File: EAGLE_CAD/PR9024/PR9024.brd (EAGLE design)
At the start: 70 x 70 mm, 71 parts, among them SW1 C&K_PTS645

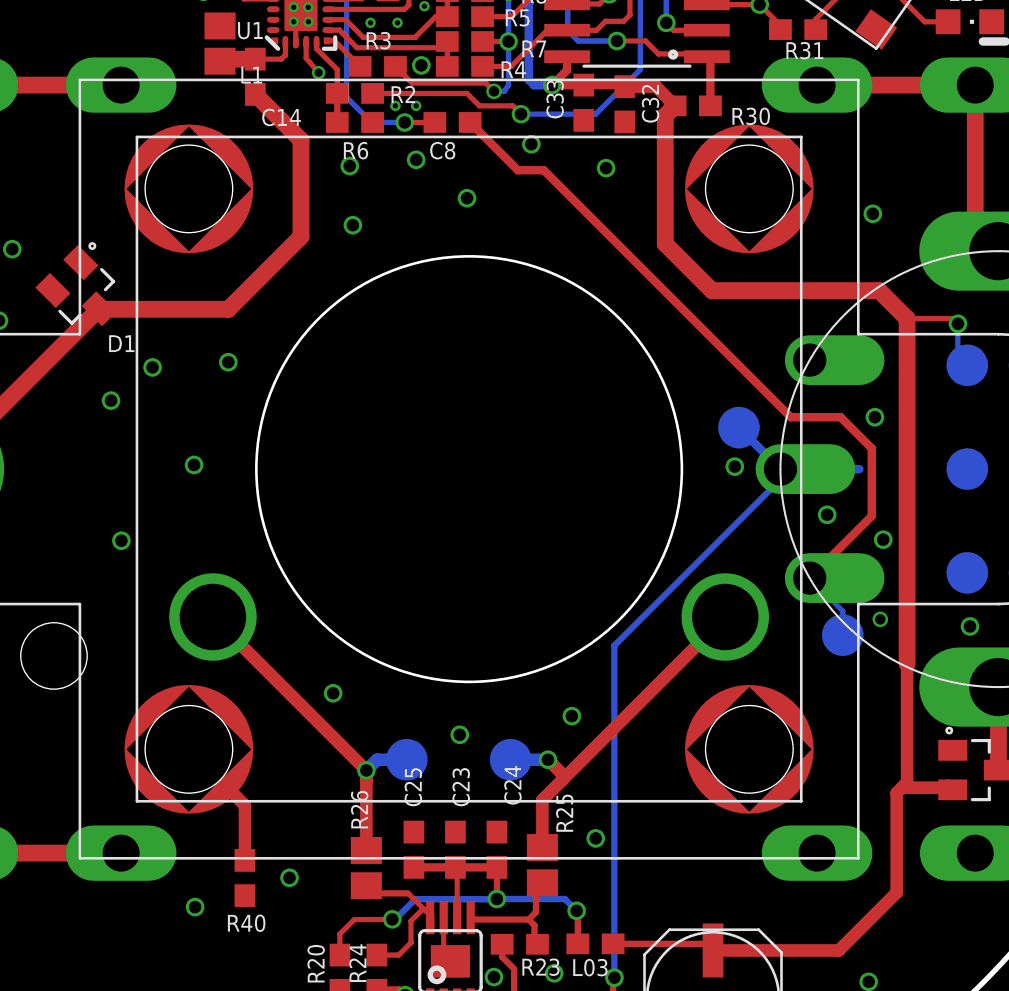
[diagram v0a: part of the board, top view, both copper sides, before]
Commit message: Updated Speaker Placement
Disconnected the SMT PEM nut placements from the speaker so the gerbers
reflect these as separate parts and placements.
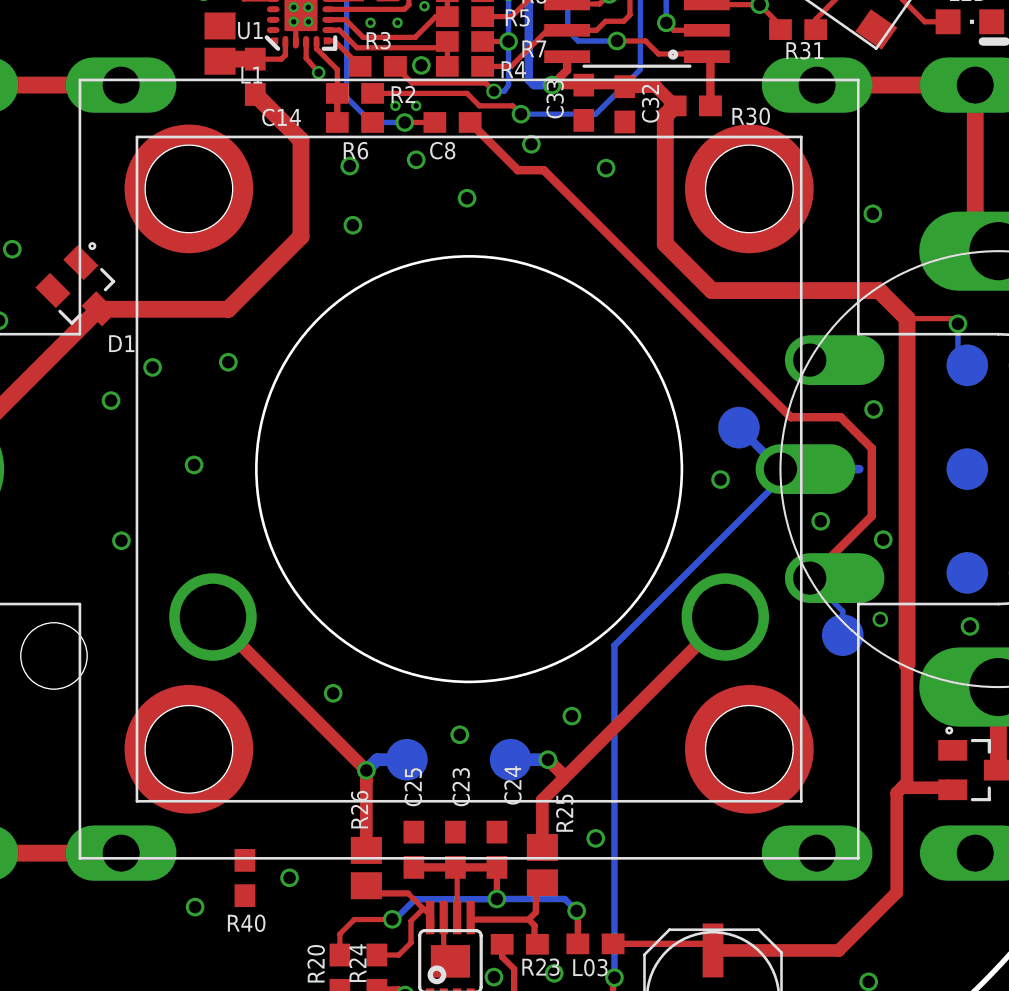
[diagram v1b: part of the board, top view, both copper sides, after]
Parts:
- added U$2, U$3, U$4, U$5: PEM_SMT, PR_Parts_Library:PEM_SMT
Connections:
- removed net N$6: R40.1, SPKR_PLACE.P$4
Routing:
- net N$6: track 6.47 -> 0.00 mm
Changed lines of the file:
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@@
 <attribute name="VALUE" x="32.336" y="14.891" size="1.27" layer="27" rot="R90"/>
 </element>
+<element name="U$2" library="PR_Parts_Library" package="PEM_SMT" value="PEM_SMT" x="21.5" y="48.5" locked="yes"/>
+<element name="U$3" library="PR_Parts_Library" package="PEM_SMT" value="PEM_SMT" x="48.5" y="48.5" locked="yes"/>
+<element name="U$4" library="PR_Parts_Library" package="PEM_SMT" value="PEM_SMT" x="48.5" y="21.5" locked="yes"/>
+<element name="U$5" library="PR_Parts_Library" package="PEM_SMT" value="PEM_SMT" x="21.5" y="21.5" locked="yes"/>
 </elements>
 <signals>
@@
 <via x="21.8" y="13.9" extent="1-16" drill="0.6"/>
 <via x="39.95" y="23.1" extent="1-16" drill="0.6"/>
-<via x="52.25" y="32.8" extent="1-16" drill="0.6"/>
+<via x="51.9375" y="32.4875" extent="1-16" drill="0.6"/>
 <via x="21.15375" y="64.95375" extent="1-16" drill="0.6"/>
 <contactref element="SW1" pad="P$1"/>
@@
 <via x="32.7" y="54.45" extent="1-16" drill="0.6"/>
 <via x="41.1" y="17.21" extent="1-16" drill="0.6"/>
-<via x="47.8" y="35.12" extent="1-16" drill="0.6"/>
-<via x="54.55" y="37.5" extent="1-16" drill="0.6"/>
+<via x="47.1125" y="34.495" extent="1-16" drill="0.6"/>
+<via x="54.4875" y="37.875" extent="1-16" drill="0.6"/>
 <via x="54.95" y="31.6" extent="1-16" drill="0.6"/>
 <via x="54.45" y="47.3" extent="1-16" drill="0.6"/>
@@
 <wire x1="30.55" y1="14.71" x2="30.7" y2="14.56" width="0.3048" layer="1"/>
 </signal>
-<signal name="N$6">
-<contactref element="SPKR_PLACE" pad="P$4"/>
-<contactref element="R40" pad="1"/>
-<wire x1="21.5" y1="21.5" x2="24.2" y2="18.8" width="0.6096" layer="1"/>
-<wire x1="24.2" y1="18.8" x2="24.2" y2="16.15" width="0.6096" layer="1"/>
-</signal>
 </signals>

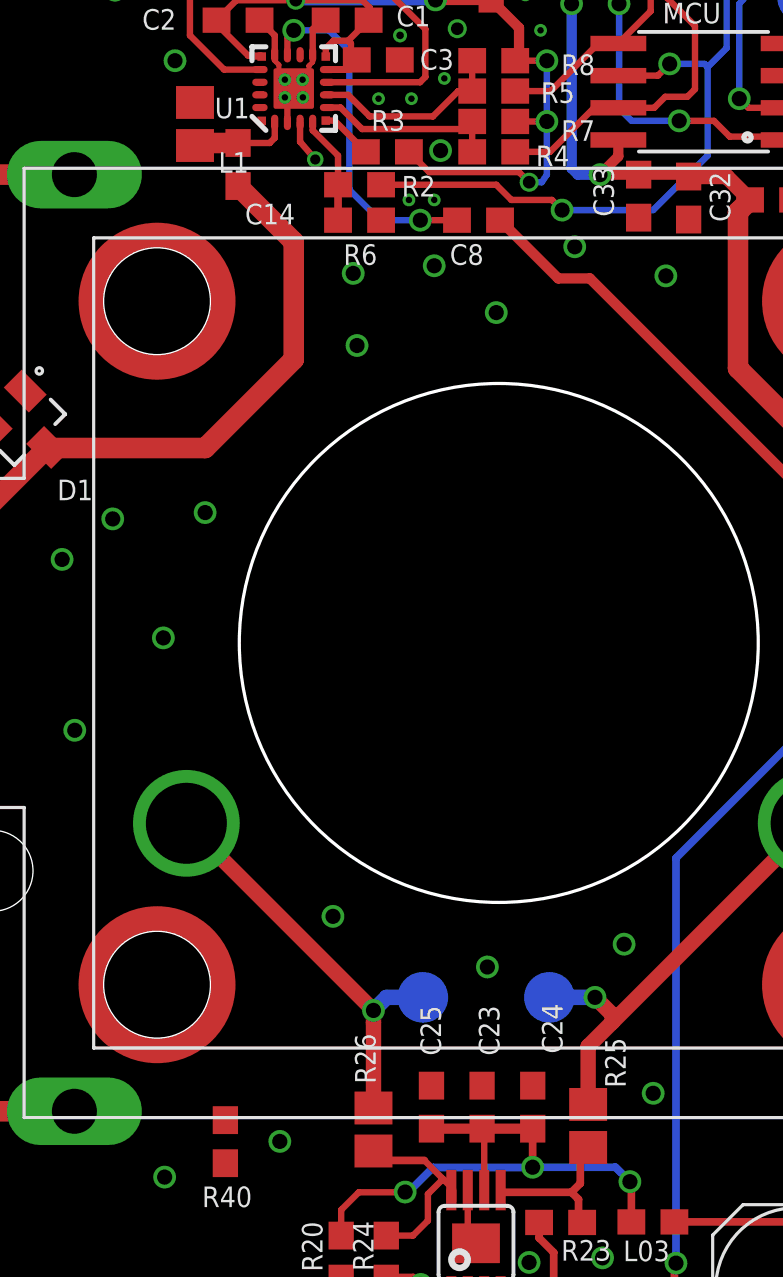
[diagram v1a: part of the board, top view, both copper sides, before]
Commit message: PR9024 & PR9001 Updates
-Small changes to PR9024
-New, simple programming board, PR9001 to connect to ISP pads and two
ground pads only.
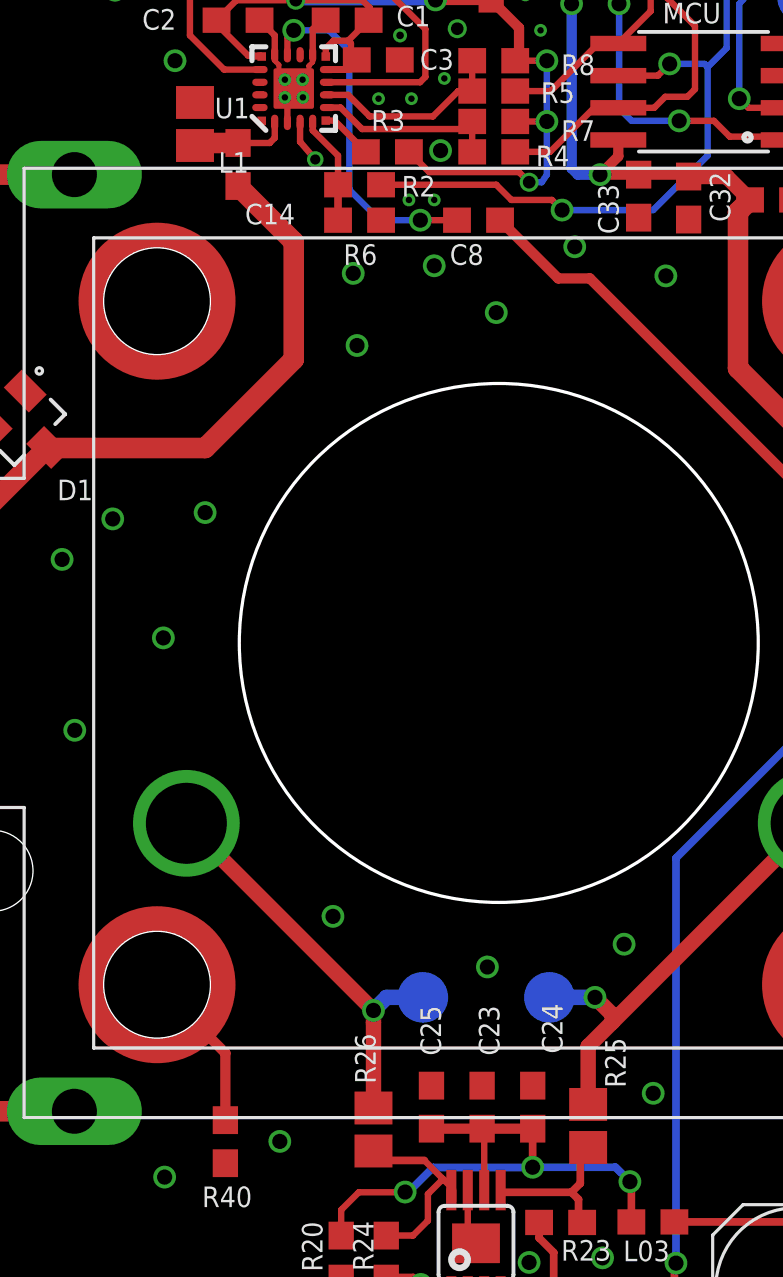
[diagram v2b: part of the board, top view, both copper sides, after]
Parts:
- U$5: value PEM_SMT -> PEM_M3_SMT_W/PIN
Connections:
- new net N$6: R40.1, U$5.P$1
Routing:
- net N$6: track 0.00 -> 6.47 mm
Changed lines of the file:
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@@
 <layer number="23" name="tOrigins" color="15" fill="1" visible="yes" active="yes"/>
 <layer number="24" name="bOrigins" color="15" fill="1" visible="yes" active="yes"/>
-<layer number="25" name="tNames" color="7" fill="1" visible="no" active="yes"/>
+<layer number="25" name="tNames" color="7" fill="1" visible="yes" active="yes"/>
 <layer number="26" name="bNames" color="7" fill="1" visible="yes" active="yes"/>
 <layer number="27" name="tValues" color="7" fill="1" visible="no" active="yes"/>
@@
 </element>
 <element name="C33" library="PR_Parts_Library" package="0603_CPL" value=".1uF" x="40.525" y="52.65" smashed="yes" rot="R270">
-<attribute name="NAME" x="39.5495" y="51.838" size="0.8128" layer="25" font="vector" ratio="16" rot="R90"/>
+<attribute name="NAME" x="39.737" y="51.1505" size="0.8128" layer="25" font="vector" ratio="16" rot="R90"/>
 <attribute name="VALUE" x="39.128" y="53.666" size="0.4064" layer="27" rot="R270"/>
 <attribute name="MFG_PN" value="CL10B104KB8SFNC" x="40.525" y="52.65" size="1.778" layer="27" rot="R270" display="off"/>
@@
 <element name="U$3" library="PR_Parts_Library" package="PEM_SMT" value="PEM_SMT" x="48.5" y="48.5" locked="yes"/>
 <element name="U$4" library="PR_Parts_Library" package="PEM_SMT" value="PEM_SMT" x="48.5" y="21.5" locked="yes"/>
-<element name="U$5" library="PR_Parts_Library" package="PEM_SMT" value="PEM_SMT" x="21.5" y="21.5" locked="yes"/>
+<element name="U$5" library="PR_Parts_Library" package="PEM_SMT" value="PEM_M3_SMT_W/PIN" x="21.5" y="21.5" locked="yes"/>
 </elements>
 <signals>
@@
 <wire x1="30.55" y1="14.71" x2="30.7" y2="14.56" width="0.3048" layer="1"/>
 </signal>
+<signal name="N$6">
+<contactref element="U$5" pad="P$1"/>
+<contactref element="R40" pad="1"/>
+<wire x1="24.2" y1="16.15" x2="24.2" y2="18.8" width="0.4064" layer="1"/>
+<wire x1="24.2" y1="18.8" x2="21.5" y2="21.5" width="0.4064" layer="1"/>
+</signal>
 </signals>
